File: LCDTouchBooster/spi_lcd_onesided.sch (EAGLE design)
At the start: 35 parts, among them IC1 MCP170312MB

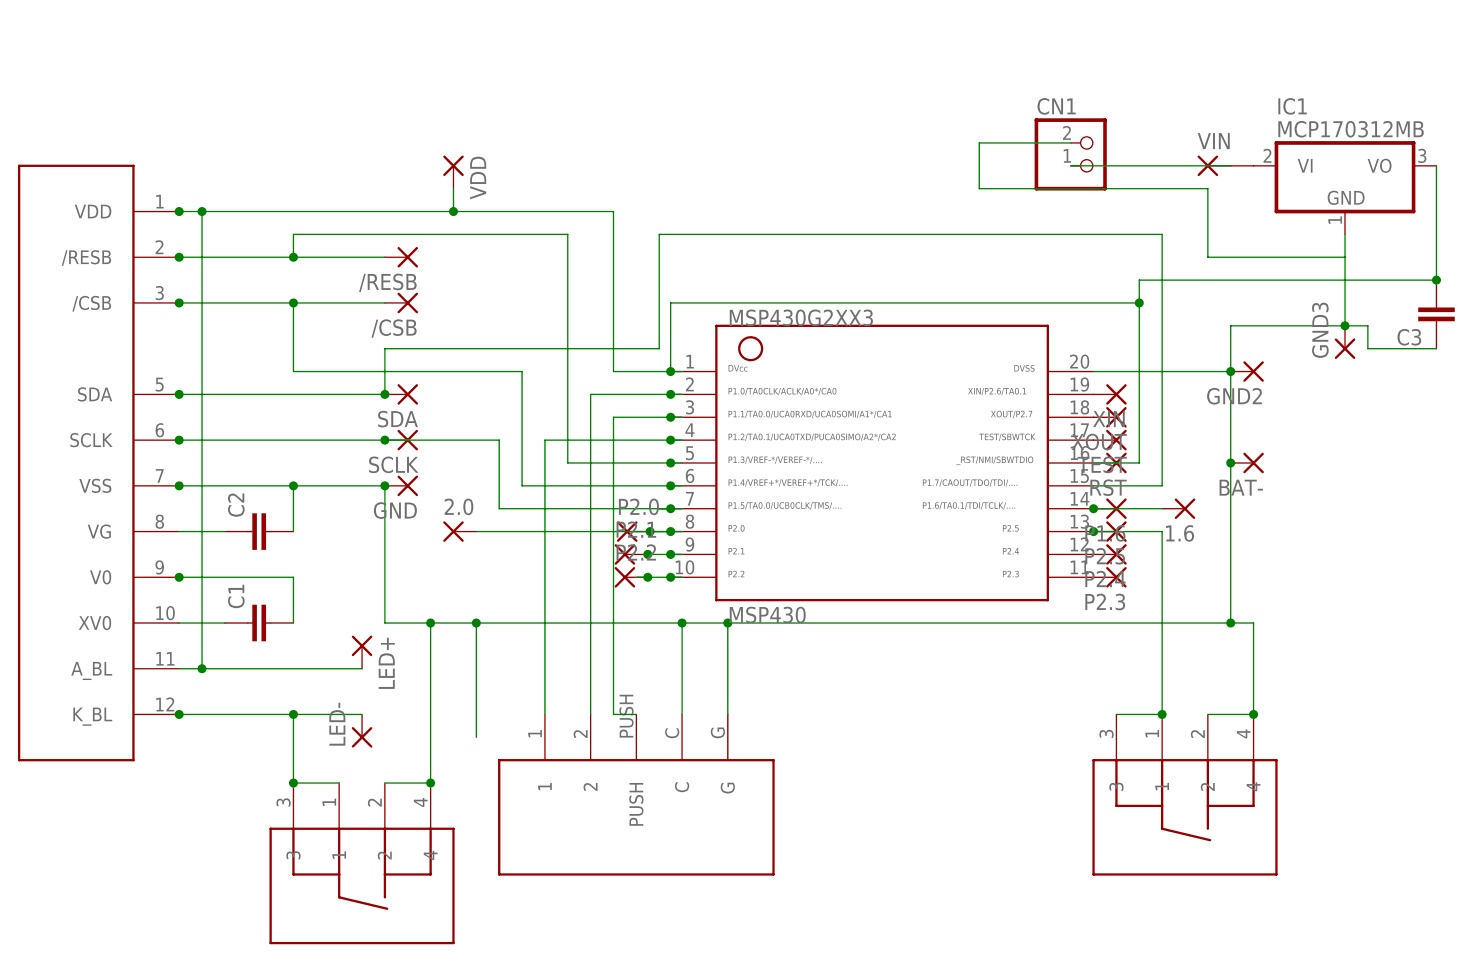
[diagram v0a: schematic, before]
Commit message: Added SPI LCD Displays
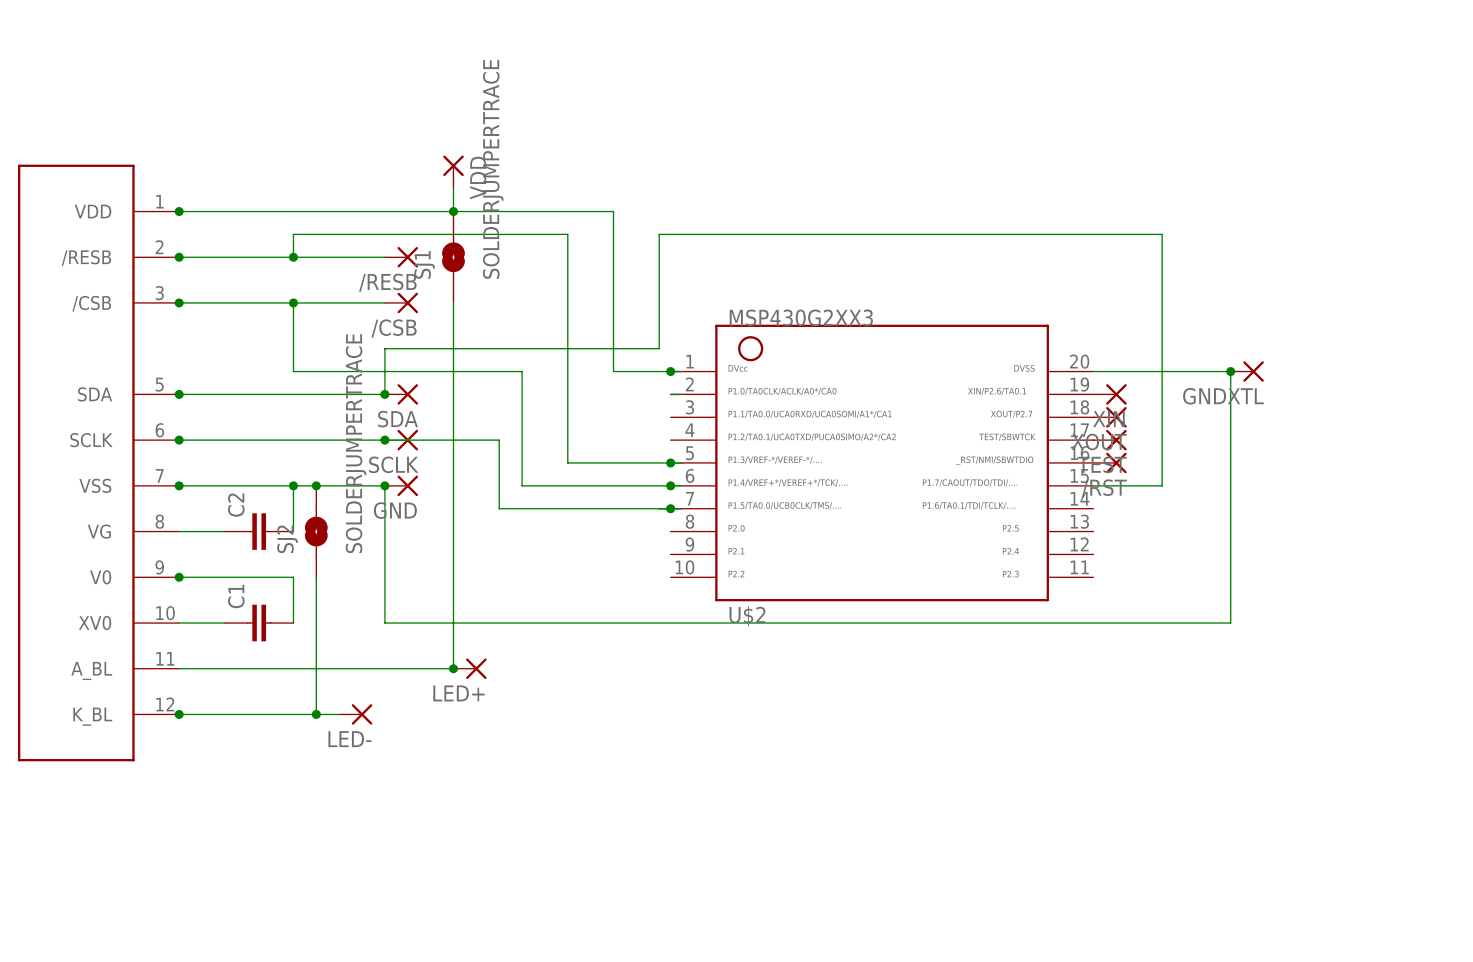
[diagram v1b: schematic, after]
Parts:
- removed 1.6, 2.0: (no value), wirepad:1,6/0,9
- removed BAT-: (no value), wirepad:SMD5
- removed C3: (no value), SparkFun-Passives:CAP0805
- removed CN1: (no value), adafruit:JST_2PIN-THM-RA
- removed GND3, P1.6, P2.0, P2.1, P2.2, P2.3, P2.4, P2.5, VIN: (no value), wirepad:SMD2
- removed IC1: MCP170312MB, linear:MCP170312MB
- removed MSP430: G2XX3---PW20, TI_MSP430_v16:G2XX3---PW20
- removed U$3: MCPL3-BC-V, apus-spidisplay:MCPL3-BC-V
- removed U$4: MCPTCF-V, apus-spidisplay:MCPTCF-V
- added SJ1, SJ2: SOLDERJUMPERTRACE, SparkFun-Passives:SOLDERJUMPERTRACE
- U$2: value MCPTCF-V -> G2XX3---PW20; device apus-spidisplay:MCPTCF-V -> TI_MSP430_v16:G2XX3---PW20
- renumbered GND2 to GNDXTL, RST to /RST
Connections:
- removed net LED-: LED-.P, U$1.K_BL, U$2.1, U$2.3
- removed net N$14: MSP430.2, U$3.2
- removed net N$15: MSP430.13, P2.5.P, U$4.1, U$4.3
- removed net N$17: MSP430.12, P2.4.P
- removed net N$18: MSP430.11, P2.3.P
- removed net N$20: MSP430.9, P2.1.P
- removed net N$21: MSP430.10, P2.2.P
- removed net N$22: 2.0.P, MSP430.8, P2.0.P
- removed net N$23: CN1.2, IC1.VI1, VIN.P
- new net N$11: TEST.P, U$2.17
- net GND: now also SJ2.2, U$2.20; no longer BAT-.P, C3.1, CN1.1, GND3.P, IC1.GND, MSP430.20, U$2.2, U$2.4, U$3.C, U$3.G, U$4.2, U$4.4
- net N$10: now also U$2.5; no longer MSP430.5
- net N$12: now also /RST.P, U$2.16; no longer MSP430.4, U$3.1
- net N$13: now also U$2.2; no longer 1.6.P, MSP430.14, P1.6.P
- net N$3: now also U$2.19; no longer MSP430.19
- net N$4: now also LED+.P, SJ1.1, U$1.A_BL; no longer MSP430.3, U$3.PUSH
- net N$5: now also LED-.P, SJ2.1, U$1.K_BL; no longer MSP430.17, TEST.P
- net N$6: now also U$2.18; no longer MSP430.18
- net N$7: now also U$2.7; no longer MSP430.7
- net N$8: now also U$2.15; no longer MSP430.15
- net N$9: now also U$2.6; no longer MSP430.6
- net VDD: now also SJ1.2, U$2.1; no longer /RST.P, C3.2, IC1.VO, LED+.P, MSP430.1, MSP430.16, U$1.A_BL
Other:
- moved on the sheet: LED+, LED-
